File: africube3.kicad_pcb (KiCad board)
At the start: 2 copper layers, 66.1 x 89.6 mm, 35 parts, among them J1 SMA Edge FM, J2 Conn_01x04, J3 RPi_GPIO, J4 Conn_01x02, U1 TQP7M9105, U2 SXBP-150+, U3 BA178M05FP-E2

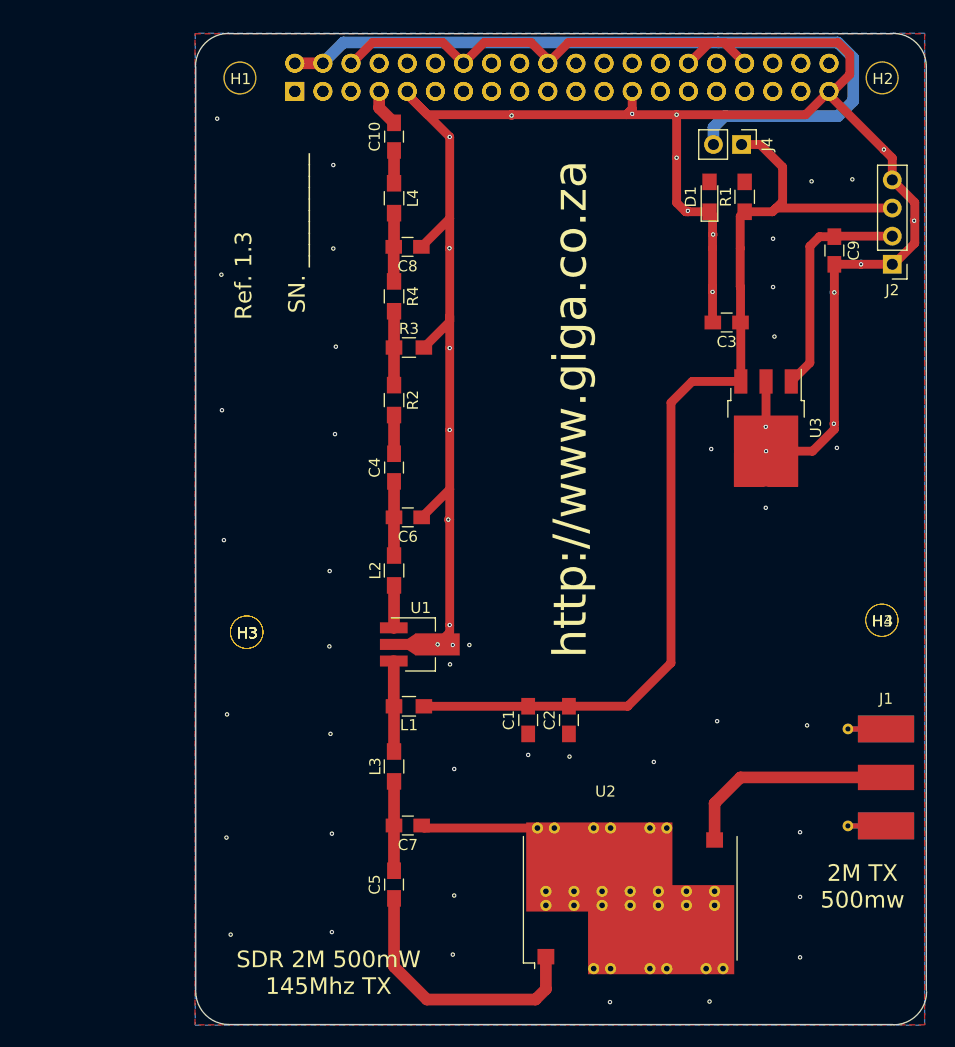
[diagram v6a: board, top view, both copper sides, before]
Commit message: updated the pcd file to africube 4 by readding inductor L5
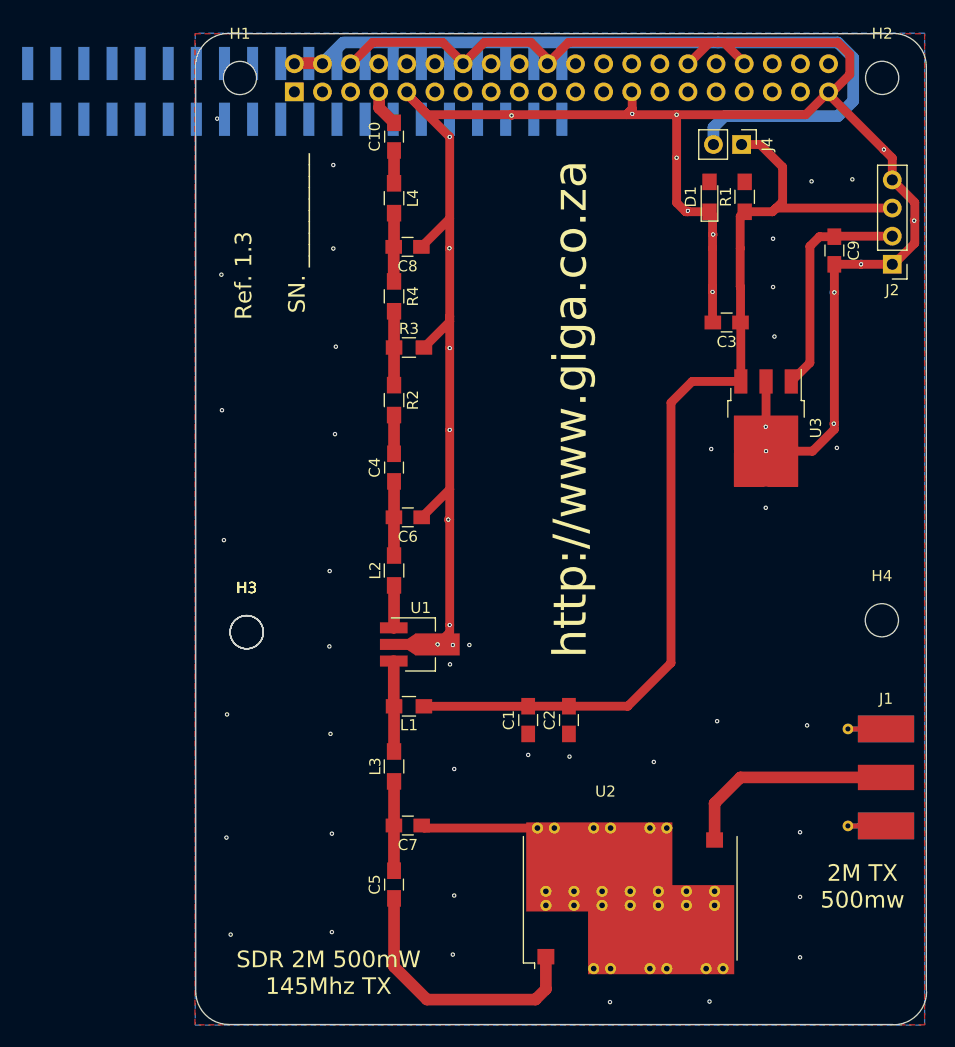
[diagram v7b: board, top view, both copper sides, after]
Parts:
- removed the H3 at (139.0, 113.3)
- removed REF**: Socket_Strip_Straight_2x20_Pitch2.54mm, pc104:Socket_Strip_Straight_2x20_Pitch2.54mm
- added J3: PinSocket_2x20_P2.54mm_Vertical, Connector_PinSocket_2.54mm:PinSocket_2x20_P2.54mm_Vertical, F.Cu at (85.9, 65.6)
- H1, H2, H3 (x4), H4: value 3mm_Mounting_Hole -> 3mm_hole; footprint project_footprints:NPTH_3mm_ID -> MountingHole:MountingHole_3mm
- J3: footprint Socket_Strips:Socket_Strip_Straight_2x20_Pitch2.54mm -> Connector_PinSocket_2.54mm:PinSocket_2x20_P2.54mm_Vertical_SMD
- L2, L3: value 2uH -> 0
- L4: value 54nH -> 0
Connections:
- J3 pad 1: (no net) -> Net-(J3-Pad1)
- J3 pad 10: (no net) -> Net-(J3-Pad10)
- J3 pad 11: (no net) -> Net-(J3-Pad11)
- J3 pad 12: (no net) -> Net-(J3-Pad12)
- J3 pad 13: (no net) -> Net-(J3-Pad13)
- J3 pad 15: (no net) -> Net-(J3-Pad15)
- J3 pad 16: (no net) -> Net-(J3-Pad16)
- J3 pad 17: (no net) -> Net-(J3-Pad17)
- J3 pad 18: (no net) -> Net-(J3-Pad18)
- J3 pad 19: (no net) -> Net-(J3-Pad19)
- J3 pad 21: (no net) -> Net-(J3-Pad21)
- J3 pad 22: (no net) -> Net-(J3-Pad22)
- J3 pad 23: (no net) -> Net-(J3-Pad23)
- J3 pad 24: (no net) -> Net-(J3-Pad24)
- J3 pad 26: (no net) -> Net-(J3-Pad26)
- J3 pad 27: (no net) -> Net-(J3-Pad27)
- J3 pad 28: (no net) -> Net-(J3-Pad28)
- J3 pad 29: (no net) -> Net-(J3-Pad29)
- J3 pad 3: (no net) -> Net-(J3-Pad3)
- J3 pad 31: (no net) -> Net-(J3-Pad31)
- J3 pad 32: (no net) -> Net-(J3-Pad32)
- J3 pad 33: (no net) -> Net-(J3-Pad33)
- J3 pad 35: (no net) -> Net-(J3-Pad35)
- J3 pad 36: (no net) -> Net-(J3-Pad36)
- J3 pad 37: (no net) -> Net-(J3-Pad37)
- J3 pad 38: (no net) -> Net-(J3-Pad38)
- J3 pad 40: (no net) -> Net-(J3-Pad40)
- J3 pad 5: (no net) -> Net-(J3-Pad5)
- J3 pad 8: (no net) -> Net-(J3-Pad8)
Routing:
- net GND: vias 61 -> 60
- net (no net): vias 0 -> 1
